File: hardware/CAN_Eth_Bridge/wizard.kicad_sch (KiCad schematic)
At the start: 44 parts, among them J301 RJ45_Amphenol_RJMG1BD3B8K1ANR, Q301 MMBT5550L, Q302 MMBT5550L, U301 W5500, Y301 Crystal_GND24

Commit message: long 88 can stick
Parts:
- removed C321: 220n, Capacitor_SMD:C_0805_2012Metric_Pad1.18x1.45mm_HandSolder, symbol Device:C_Small
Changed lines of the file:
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@@
 	)
 	(junction
-		(at 34.29 27.94)
-		(diameter 0)
-		(color 0 0 0 0)
-	)
-	(junction
 		(at 91.44 27.94)
 		(diameter 0)
@@
 	)
 	(junction
-		(at 34.29 33.02)
-		(diameter 0)
-		(color 0 0 0 0)
-	)
-	(junction
 		(at 81.28 114.3)
 		(diameter 0)
@@
 	(wire
 		(pts
-			(xy 34.29 33.02) (xy 44.45 33.02)
+			(xy 26.67 33.02) (xy 44.45 33.02)
 		)
 		(stroke
@@
 	(wire
 		(pts
-			(xy 26.67 33.02) (xy 34.29 33.02)
-		)
-		(stroke
-			(width 0)
-			(type default)
-		)
-	)
-	(wire
-		(pts
 			(xy 182.88 77.47) (xy 182.88 81.28)
 		)
@@
 	(wire
 		(pts
-			(xy 26.67 27.94) (xy 34.29 27.94)
-		)
-		(stroke
-			(width 0)
-			(type default)
-		)
-	)
-	(wire
-		(pts
 			(xy 91.44 139.7) (xy 105.41 139.7)
 		)
@@
 	(wire
 		(pts
-			(xy 34.29 27.94) (xy 44.45 27.94)
+			(xy 26.67 27.94) (xy 44.45 27.94)
 		)
 		(stroke
@@
 					(unit 1)
 				)
-			)
-		)
-	)
-	(symbol
-		(lib_id "Device:C_Small")
-		(at 34.29 30.48 0)
-		(unit 1)
-		(exclude_from_sim no)
-		(in_bom yes)
-		(on_board yes)
-		(dnp no)
-		(property "Reference" "C321"
-			(at 36.83 29.2162 0)
-			(effects
-				(font
-					(size 1.27 1.27)
-				)
-				(justify left)
-			)
-		)
-		(property "Value" "220n"
-			(at 36.83 31.7562 0)
-			(effects
-				(font
-					(size 1.27 1.27)
-				)
-				(justify left)
-			)
-		)
-		(property "Footprint" "Capacitor_SMD:C_0805_2012Metric_Pad1.18x1.45mm_HandSolder"
-			(at 34.29 30.48 0)
-			(effects
-				(font
-					(size 1.27 1.27)
-				)
-				(hide yes)
-			)
-		)
-		(property "Datasheet" "https://www.mouser.com/ProductDetail/Samsung-Electro-Mechanics/CL31B224KBFNNNF?qs=sGAEpiMZZMsh%252B1woXyUXj7iNKXiFkBmw7C%252BUlKpuDJ8%3D"
-			(at 34.29 30.48 0)
-			(effects
-				(font
-					(size 1.27 1.27)
-				)
-				(hide yes)
-			)
-		)
-		(property "Description" ""
-			(at 34.29 30.48 0)
-			(effects
-				(font
-					(size 1.27 1.27)
-				)
-				(hide yes)
-			)
-		)
-		(property "Sim.Device" ""
-			(at 34.29 30.48 0)
-			(effects
-				(font
-					(size 1.27 1.27)
-				)
-				(hide yes)
-			)
-		)
-		(property "Sim.Type" ""
-			(at 34.29 30.48 0)
-			(effects
-				(font
-					(size 1.27 1.27)
-				)
-				(hide yes)
-			)
-		)
-		(property "mouser" "https://www.mouser.com/ProductDetail/Samsung-Electro-Mechanics/CL21B224KCFSFNE?qs=664zcAxDQ0l4Y1eUk6Zc1g%3D%3D"
-			(at 34.29 30.48 0)
-			(effects
-				(font
-					(size 1.27 1.27)
-				)
-				(hide yes)
-			)
-		)
-		(property "specs" "100VDC, X7R, 10%, -55C, +125C, 220nF"
-			(at 34.29 30.48 0)
-			(effects
-				(font
-					(size 1.27 1.27)
-				)
-				(hide yes)
-			)
-		)
-		(property "unit x10" "0.054"
-			(at 34.29 30.48 0)
-			(effects
-				(font
-					(size 1.27 1.27)
-				)
-				(hide yes)
-			)
-		)
-		(property "Sim.Pins" ""
-			(at 34.29 30.48 0)
-			(effects
-				(font
-					(size 1.27 1.27)
-				)
-				(hide yes)
-			)
-		)
-		(property "note" ""
-			(at 34.29 30.48 0)
-			(effects
-				(font
-					(size 1.27 1.27)
-				)
-				(hide yes)
-			)
-		)
-		(pin "2"
-		)
-		(pin "1"
-		)
-		(instances
-			(project "MasterBoard_A"
-				(path "/20ac6af0-79b5-4ba6-aad3-75081d02c913/ecddfaa5-574e-47c9-961e-691ad3df8c33"
-					(reference "C321")
-					(unit 1)
-				)

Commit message: hdd failure D:
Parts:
- removed C307, C308, C310: 100n, Capacitor_SMD:C_0603_1608Metric_Pad1.08x0.95mm_HandSolder, symbol Device:C_Small
- removed C315: 220n, Capacitor_SMD:C_0805_2012Metric_Pad1.18x1.45mm_HandSolder, symbol Device:C_Small
- removed R304, R305, R307, R308: 14.3, Resistor_SMD:R_0805_2012Metric_Pad1.20x1.40mm_HandSolder, symbol Device:R_Small_US
- removed R306: 10, Resistor_SMD:R_0805_2012Metric_Pad1.20x1.40mm_HandSolder, symbol Device:R_Small_US
- R311, R312: value 4.99k -> 3.32k; footprint Resistor_SMD:R_1206_3216Metric_Pad1.30x1.75mm_HandSolder -> Resistor_SMD:R_0805_2012Metric_Pad1.20x1.40mm_HandSolder; mouser https://www.mouser.com/ProductDetail/SEI-Stackpole/RNCP1206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 -> https://www.mouser.com/ProductDetail/Walsin/WR08X3321FTL?qs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; specs 4.99kOhm, 200V, 500mW, 1%, 100PPM, -55C, +155C -> 3.32kOhm, 1%, 150V, 125mW, 100ppm, -55C, 155C; unit x1 0.1 -> 0.10; unit x10 0.016 -> 0.019
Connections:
- net RX_1+ is gone; now on net RX+: C316.1, R314.2
- net RX_1- is gone; now on net RX-: C317.1, R310.2
- net TX+ is gone; now on net TD+: U301.2 (TXP)
- net TX- is gone; now on net TD-: U301.1 (TXN)

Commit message: kil!
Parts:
- R302: value 14.3 -> 10; mouser https://www.mouser.com/ProductDetail/KOA-Speer/RK73H2ATTD14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 -> https://www.mouser.com/ProductDetail/KOA-Speer/RK73H2ATTD10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; specs 14.3R, 250mW, 1%, 100ppm, 150V, -55C, +155C -> 10R, 150V, 250mW, 1%, 100ppm, -55C, +155C
- R311, R312: value 3.32k -> 2.4k; mouser https://www.mouser.com/ProductDetail/Walsin/WR08X3321FTL?qs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 -> https://www.mouser.com/ProductDetail/Panasonic/ERJ-P06J242V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; specs 3.32kOhm, 1%, 150V, 125mW, 100ppm, -55C, 155C -> (none); specs  (none) -> 500mW, 5%, 200ppm, 400V, -55C, +155C, anti-surge, TF; unit x1 0.10 -> 0.12; unit x10 0.019 -> 0.039
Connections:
- net at U301.25 (LINKLED): now also R311.2; no longer R311.1
- net at R312.1: now also Q302.1 (B); no longer U301.27 (ACTLED)
- net at R312.2: now also U301.27 (ACTLED); no longer Q302.1 (B)
- net at Q301.1 (B): now also R311.1; no longer R311.2

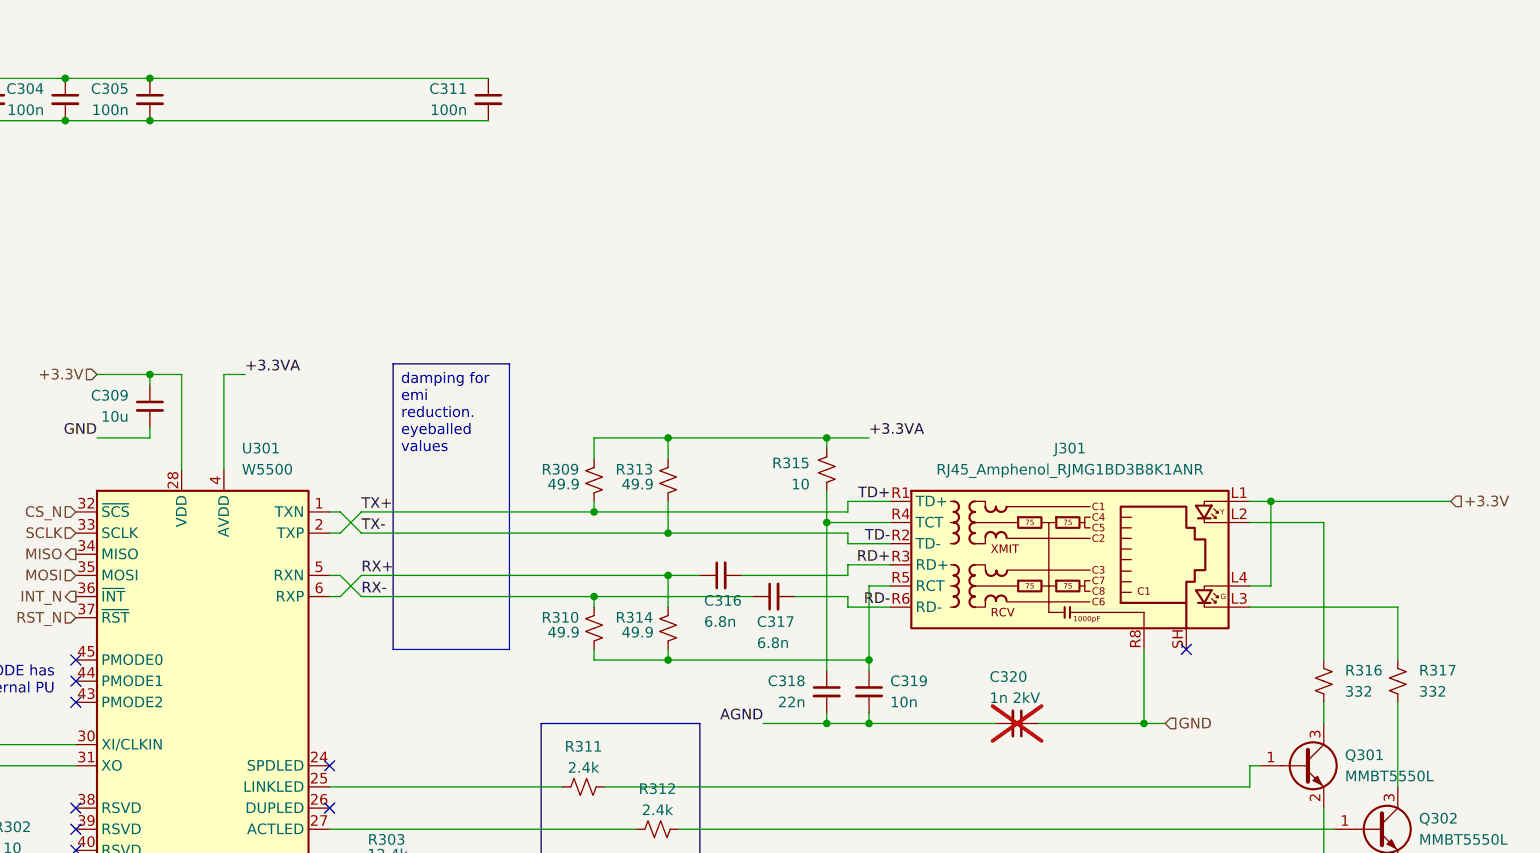
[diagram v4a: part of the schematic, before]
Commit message: super 3v3 rail
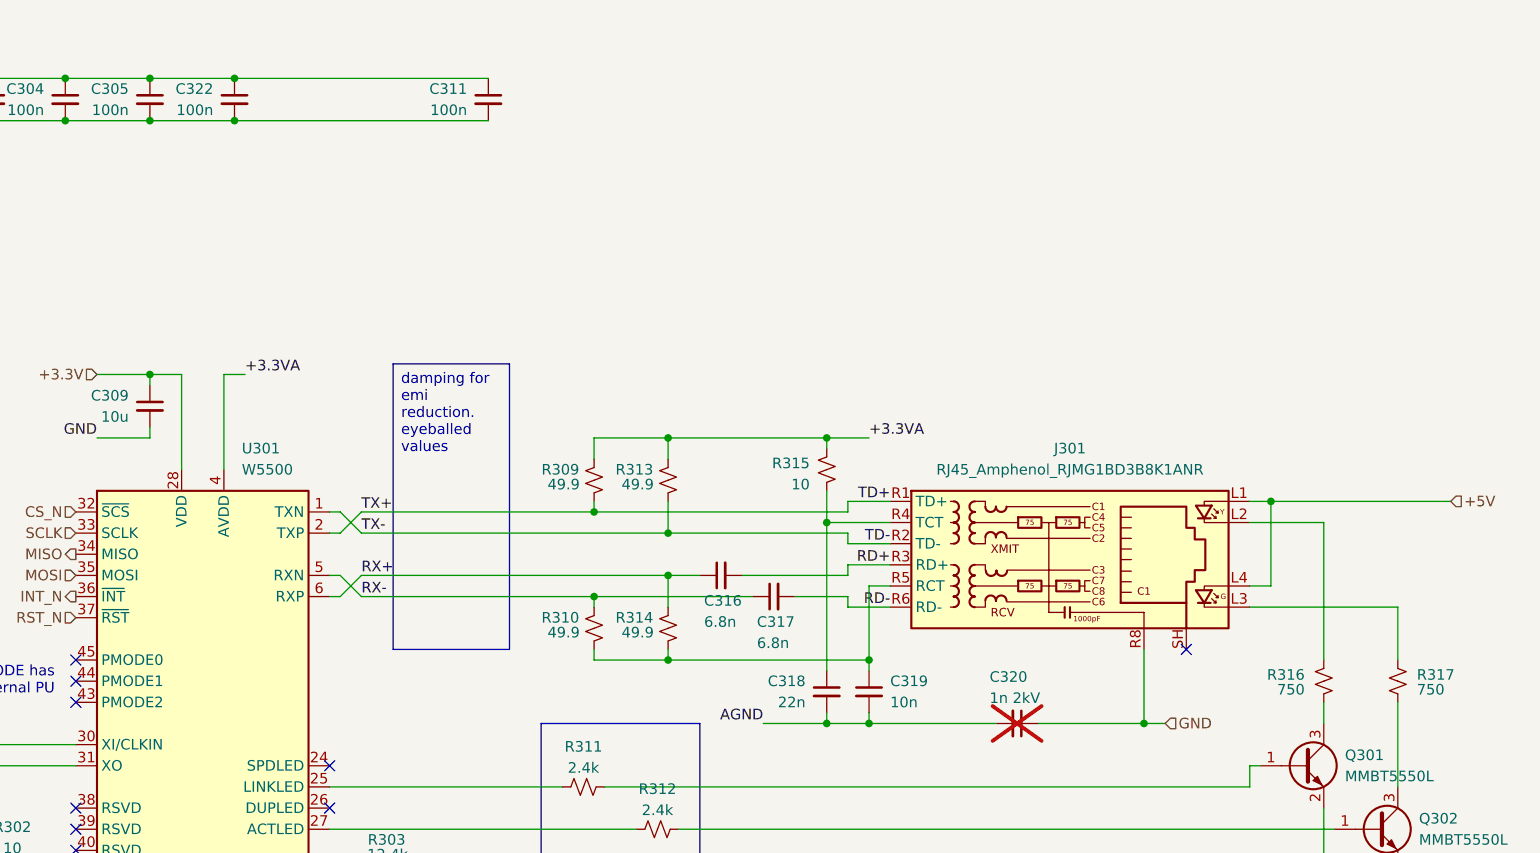
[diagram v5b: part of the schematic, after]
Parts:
- added C322: 100n, Capacitor_SMD:C_0603_1608Metric_Pad1.08x0.95mm_HandSolder, symbol Device:C_Small
- R316, R317: value 332 -> 750; mouser https://www.mouser.com/ProductDetail/YAGEO/AC1206FR-07332RL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 -> https://www.mouser.com/ProductDetail/YAGEO/RC1206JR-13750RL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; specs 332 ohm, 250mW, 200V, 1%, 100ppm, -55C, +155C -> 750mOhm, 250mW, 5%, 100PPM, 200C, -55C, +155C; unit x1 0.10 -> 0.1; unit x10 0.016 -> 0.022
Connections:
- net +3.3V: no longer J301.L1, J301.L4
- net +3.3VA: now also C322.1
- net GND: now also C322.2
- net at R317.1: now also Q302.3 (C); no longer J301.L3
- net at R317.2: now also J301.L3; no longer Q302.3 (C)
- new net +5V: J301.L1, J301.L4

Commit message: commented
software skill issue? hardware looks fine
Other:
- note added: "base low: carrier sense detected"
- note added: "base low: link established"
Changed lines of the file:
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@@
+		)
+	)
+	(text "base low: carrier sense detected"
+		(exclude_from_sim no)
+		(at 232.664 116.586 0)
+		(effects
+			(font
+				(size 1.27 1.27)
+				(color 194 0 194 1)
+			)
+			(justify right top)
+		)
+	)
+	(text "base low: link established"
+		(exclude_from_sim no)
+		(at 232.664 110.744 0)
+		(effects
+			(font
+				(size 1.27 1.27)
+				(color 194 0 194 1)
+			)
+			(justify right top)
 		)
 	)
@@
 	(text_box "damping for emi reduction. eyeballed values"
 		(exclude_from_sim no)
-		(at 130.81 62.23 0)
+		(at 132.08 62.23 0)
 		(size 13.97 34.29)
 		(margins 0.9525 0.9525 0.9525 0.9525)

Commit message: lsoing it
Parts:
- removed C322: 100n, Capacitor_SMD:C_0603_1608Metric_Pad1.08x0.95mm_HandSolder, symbol Device:C_Small
- C301: value 10u -> 220n; footprint Capacitor_SMD:C_1206_3216Metric_Pad1.33x1.80mm_HandSolder -> Capacitor_SMD:C_0805_2012Metric_Pad1.18x1.45mm_HandSolder; mouser https://www.mouser.com/ProductDetail/Samsung-Electro-Mechanics/CL31A106KBHNNNE?qs=sGAEpiMZZMsh%252B1woXyUXjxqcB7t9naYpzWmpMbMJIKQ%3D -> https://www.mouser.com/ProductDetail/Samsung-Electro-Mechanics/CL21B224KCFSFNE?qs=664zcAxDQ0l4Y1eUk6Zc1g%3D%3D; specs 10uF, 50VDC, X5R, 10%, -55C, +85C -> 100VDC, X7R, 10%, -55C, +125C, 220nF; unit x1 (none) -> 0.054; unit x10 0.07 -> 0.054
- C302, C309: value 10u -> 22u; footprint Capacitor_SMD:C_1206_3216Metric_Pad1.33x1.80mm_HandSolder -> Capacitor_SMD:C_0805_2012Metric_Pad1.18x1.45mm_HandSolder; mouser https://www.mouser.com/ProductDetail/Samsung-Electro-Mechanics/CL31A106KBHNNNE?qs=sGAEpiMZZMsh%252B1woXyUXjxqcB7t9naYpzWmpMbMJIKQ%3D -> https://www.mouser.com/ProductDetail/Samsung-Electro-Mechanics/CL21A226MAYNNNE?qs=sGAEpiMZZMsh%252B1woXyUXj9e2R%2FOkAO5o4FNiyGuFzx8%3D; specs 10uF, 50VDC, X5R, 10%, -55C, +85C -> 22uF, 25V, 20%, X5R, -55C, +85C; unit x10 0.07 -> 0.043
- C304, C305, C311: value 100n -> 220n; footprint Capacitor_SMD:C_0603_1608Metric_Pad1.08x0.95mm_HandSolder -> Capacitor_SMD:C_0805_2012Metric_Pad1.18x1.45mm_HandSolder; mouser https://www.mouser.com/ProductDetail/Wurth-Elektronik/88501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 -> https://www.mouser.com/ProductDetail/Samsung-Electro-Mechan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; specs 100nF, 10%, 50V, X7R, -55C, +125C -> 100VDC, X7R, 10%, -55C, +125C, 220nF; unit x1 0.10 -> 0.054; unit x10 0.029 -> 0.054; unit x100 0.017 -> (none); unit x50 0.02 -> (none)
- R301: footprint Resistor_SMD:R_0603_1608Metric_Pad0.98x0.95mm_HandSolder -> Resistor_SMD:R_0805_2012Metric_Pad1.20x1.40mm_HandSolder; mouser https://www.mouser.com/ProductDetail/Bourns/CRT0603-DZ-1004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 -> https://www.mouser.com/ProductDetail/Vishay-Beyschlag/MCU08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; specs 1M, 100mW, 750V, 0.5%, 50ppm, -55C, +155C -> 1M, 125mW, 150V, 1%, 50ppm, -55C, +125C; unit x1 0.10 -> 0.1; unit x10 0.031 -> 0.067

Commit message: updated 3d models
freecad my belovid
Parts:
- J301: footprint Connector_RJ:RJ45_Amphenol_RJMG1BD3B8K1ANR -> zzLocalLibraries-Footprints:RJ45_Amphenol_RJMG1BD3B8K1ANR
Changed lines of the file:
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@@
 			)
 		)
-		(property "Footprint" "Connector_RJ:RJ45_Amphenol_RJMG1BD3B8K1ANR"
+		(property "Footprint" "zzLocalLibraries-Footprints:RJ45_Amphenol_RJMG1BD3B8K1ANR"
 			(at 210.82 73.66 0)
 			(effects
